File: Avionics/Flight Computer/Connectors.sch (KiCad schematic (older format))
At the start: 3 parts, among them J1 ERF8-040-05.0-S-DV-K, J2 ERF8-040-05.0-S-DV-K, J3 473460001

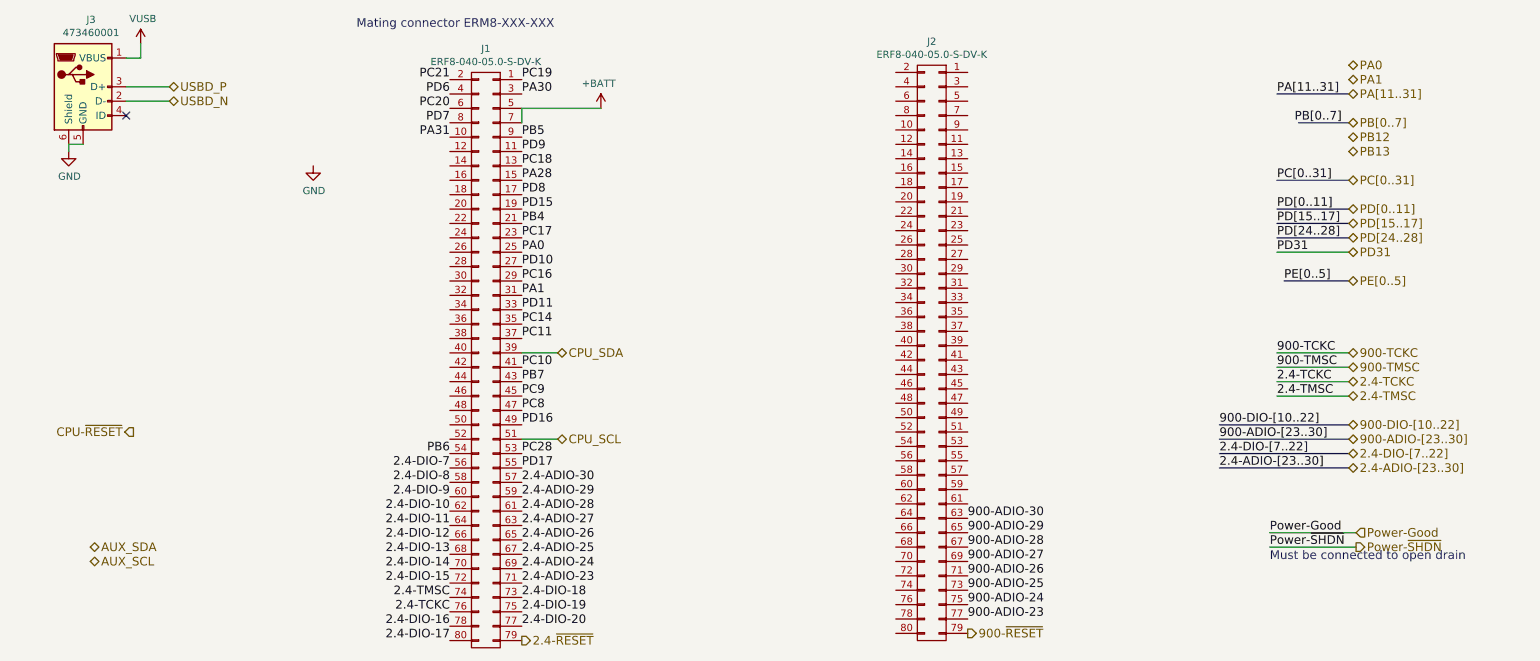
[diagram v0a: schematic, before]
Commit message: Additional routing
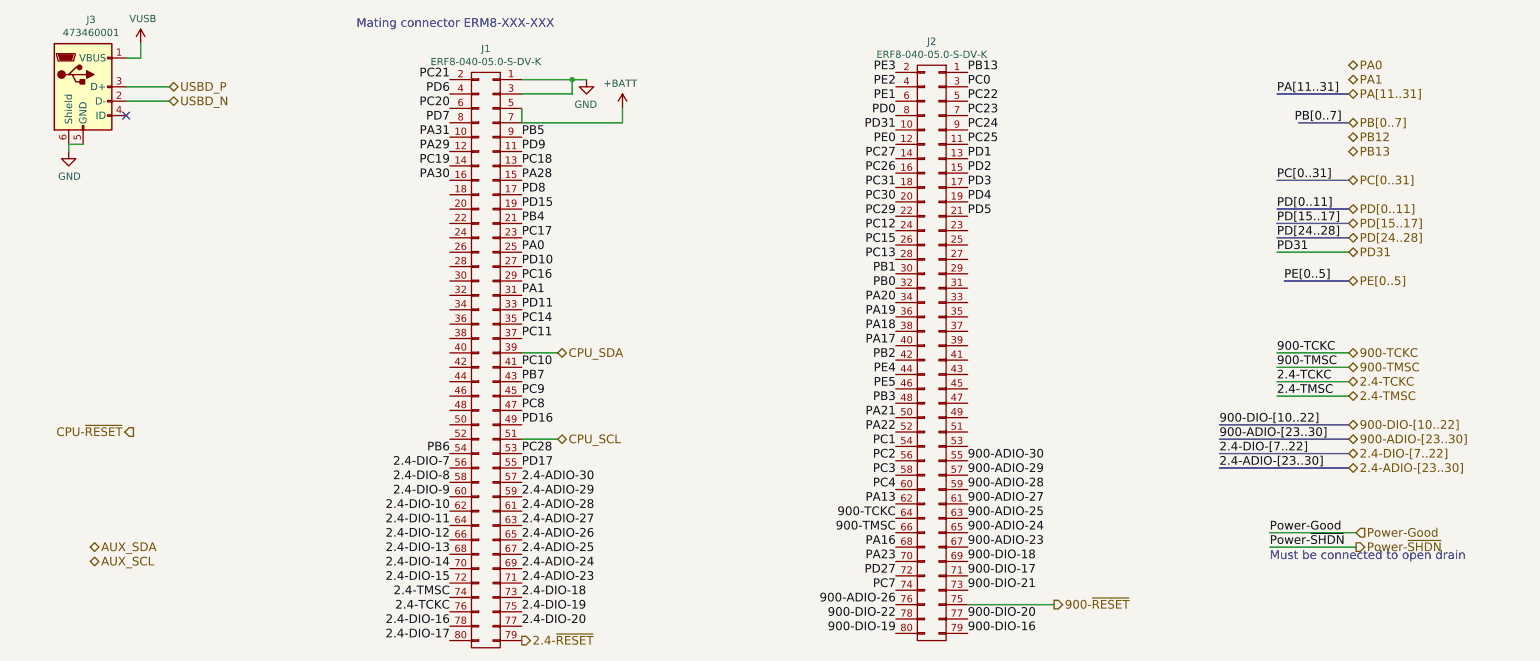
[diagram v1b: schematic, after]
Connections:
- net 900-ADIO-23: now also J2.67 (P67); no longer J2.77 (P77)
- net 900-ADIO-24: now also J2.65 (P65); no longer J2.75 (P75)
- net 900-ADIO-25: now also J2.63 (P63); no longer J2.73 (P73)
- net 900-ADIO-26: now also J2.76 (P76); no longer J2.71 (P71)
- net 900-ADIO-27: now also J2.61 (P61); no longer J2.69 (P69)
- net 900-ADIO-28: now also J2.59 (P59); no longer J2.67 (P67)
- net 900-ADIO-29: now also J2.57 (P57); no longer J2.65 (P65)
- net 900-ADIO-30: now also J2.55 (P55); no longer J2.63 (P63)
- net 900-TCKC: now also J2.64 (P64)
- net 900-TMSC: now also J2.66 (P66)
- net 900-~RESET: now also J2.75 (P75); no longer J2.79 (P79)
- net GND: now also J1.1 (P1), J1.3 (P3)
- net PA30: now also J1.16 (P16); no longer J1.3 (P3)
- net PB13: now also J2.1 (P1)
- net PC19: now also J1.14 (P14); no longer J1.1 (P1)
- net PD31: now also J2.10 (P10)
- net PC25: now reaches J2.11 (P11)
- net PE0: now reaches J2.12 (P12)
- net PD1: now reaches J2.13 (P13)
- net PC27: now reaches J2.14 (P14)
- net PD2: now reaches J2.15 (P15)
- net PC26: now reaches J2.16 (P16)
- net PD3: now reaches J2.17 (P17)
- net PC31: now reaches J2.18 (P18)
- net PD4: now reaches J2.19 (P19)
- net PE3: now reaches J2.2 (P2)
- net PC30: now reaches J2.20 (P20)
- net PD5: now reaches J2.21 (P21)
- net PC29: now reaches J2.22 (P22)
- net PC12: now reaches J2.24 (P24)
- net PC15: now reaches J2.26 (P26)
- net PC13: now reaches J2.28 (P28)
- net PC0: now reaches J2.3 (P3)
- net PB1: now reaches J2.30 (P30)
- net PB0: now reaches J2.32 (P32)
- net PA20: now reaches J2.34 (P34)
- net PA19: now reaches J2.36 (P36)
- net PA18: now reaches J2.38 (P38)
- net PE2: now reaches J2.4 (P4)
- net PA17: now reaches J2.40 (P40)
- net PB2: now reaches J2.42 (P42)
- net PE4: now reaches J2.44 (P44)
- net PE5: now reaches J2.46 (P46)
- net PB3: now reaches J2.48 (P48)
- net PC22: now reaches J2.5 (P5)
- net PA21: now reaches J2.50 (P50)
- net PA22: now reaches J2.52 (P52)
- net PC1: now reaches J2.54 (P54)
- net PC2: now reaches J2.56 (P56)
- net PC3: now reaches J2.58 (P58)
- net PE1: now reaches J2.6 (P6)
- net PC4: now reaches J2.60 (P60)
- net PA13: now reaches J2.62 (P62)
- net PA16: now reaches J2.68 (P68)
- net PC23: now reaches J2.7 (P7)
- net PA23: now reaches J2.70 (P70)
- net PD27: now reaches J2.72 (P72)
- net PC7: now reaches J2.74 (P74)
- net 900-DIO-22: now reaches J2.78 (P78)
- net PD0: now reaches J2.8 (P8)
- net 900-DIO-19: now reaches J2.80 (P80)
- net PC24: now reaches J2.9 (P9)
- net PA29: now reaches J1.12 (P12)
- new net 900-DIO-16: J2.79 (P79)
- new net 900-DIO-17: J2.71 (P71)
- new net 900-DIO-18: J2.69 (P69)
- new net 900-DIO-20: J2.77 (P77)
- new net 900-DIO-21: J2.73 (P73)
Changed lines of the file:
@@
 Text HLabel 1550 3850 0    60   Output ~ 0
 CPU-~RESET
-Text HLabel 7350 5250 2    60   Output ~ 0
+Text HLabel 7950 5050 2    60   Output ~ 0
 900-~RESET
 Text HLabel 4250 5300 2    60   Output ~ 0
@@
 Text Notes 9450 4750 0    60   ~ 0
 Must be connected to open drain\n
-Wire Wire Line
-	4800 1600 4250 1600
 $Comp
 L +BATT #PWR0118
 U 1 1 58DB91A4
-P 4800 1600
-F 0 "#PWR0118" H 3750 -1300 50  0001 C CNN
-F 1 "+BATT" H 4815 1773 50  0000 C CNN
-F 2 "" H 3750 -1150 50  0001 C CNN
-F 3 "" H 3750 -1150 50  0001 C CNN
-	1    4800 1600
+P 4950 1600
+F 0 "#PWR0118" H 3900 -1300 50  0001 C CNN
+F 1 "+BATT" H 4965 1773 50  0000 C CNN
+F 2 "" H 3900 -1150 50  0001 C CNN
+F 3 "" H 3900 -1150 50  0001 C CNN
+	1    4950 1600
 	-1   0    0    -1
 $EndComp
@@
 L GND #PWR0119
 U 1 1 58DD26EA
-P 2800 2000
-F 0 "#PWR0119" H -1150 -1700 50  0001 C CNN
-F 1 "GND" H 2805 1827 50  0000 C CNN
-F 2 "" H -1150 -1450 50  0001 C CNN
-F 3 "" H -1150 -1450 50  0001 C CNN
-	1    2800 2000
-	1    0    0    -1
+P 4700 1400
+F 0 "#PWR0119" H 750 -2300 50  0001 C CNN
+F 1 "GND" H 4705 1227 50  0000 C CNN
+F 2 "" H 750 -2050 50  0001 C CNN
+F 3 "" H 750 -2050 50  0001 C CNN
+	1    4700 1400
+	-1   0    0    -1
 $EndComp
+Text Label 7350 4150 0    60   ~ 0
+900-ADIO-29
+Text Label 7350 4050 0    60   ~ 0
+900-ADIO-30
+Text Label 7350 4250 0    60   ~ 0
+900-ADIO-28
+Text Label 6850 5050 2    60   ~ 0
+900-ADIO-26
 Text Label 7350 4550 0    60   ~ 0
-900-ADIO-29
+900-ADIO-24
+Text Label 7350 4650 0    60   ~ 0
+900-ADIO-23
+Text Label 7350 4350 0    60   ~ 0
+900-ADIO-27
 Text Label 7350 4450 0    60   ~ 0
-900-ADIO-30
-Text Label 7350 4650 0    60   ~ 0
-900-ADIO-28
-Text Label 7350 4850 0    60   ~ 0
-900-ADIO-26
-Text Label 7350 5050 0    60   ~ 0
-900-ADIO-24
-Text Label 7350 5150 0    60   ~ 0
-900-ADIO-23
-Text Label 7350 4750 0    60   ~ 0
-900-ADIO-27
-Text Label 7350 4950 0    60   ~ 0
 900-ADIO-25
 Text Label 3750 4200 2    60   ~ 0
@@
 Text Label 4250 1800 0    60   ~ 0
 PB5
-Text Label 4250 1500 0    60   ~ 0
+Text Label 3750 2100 2    60   ~ 0
 PA30
-Text Label 4250 1400 0    60   ~ 0
+Text Label 3750 2000 2    60   ~ 0
 PC19
 Text Label 3750 1800 2    60   ~ 0
@@
 Text Label 3750 1400 2    60   ~ 0
 PC21
+Text Label 6850 1350 2    60   ~ 0
+PE3
+Text Label 6850 1450 2    60   ~ 0
+PE2
+Text Label 6850 1550 2    60   ~ 0
+PE1
+Text Label 6850 1650 2    60   ~ 0
+PD0
+Text Label 6850 1750 2    60   ~ 0
+PD31
+Text Label 6850 1850 2    60   ~ 0
+PE0
+Text Label 7350 1350 0    60   ~ 0
+PB13
+Text Label 7350 1450 0    60   ~ 0
+PC0
+Text Label 6850 1950 2    60   ~ 0
+PC27
+Text Label 6850 2050 2    60   ~ 0
+PC26
+Text Label 6850 2150 2    60   ~ 0
+PC31
+Text Label 6850 2250 2    60   ~ 0
+PC30
+Text Label 6850 2350 2    60   ~ 0
+PC29
+Text Label 6850 2450 2    60   ~ 0
+PC12
+Text Label 6850 2550 2    60   ~ 0
+PC15
+Text Label 6850 2650 2    60   ~ 0
+PC13
+Text Label 6850 2750 2    60   ~ 0
+PB1
+Text Label 6850 2850 2    60   ~ 0
+PB0
+Text Label 6850 2950 2    60   ~ 0
+PA20
+Text Label 6850 3050 2    60   ~ 0
+PA19
+Text Label 6850 3150 2    60   ~ 0
+PA18
+Text Label 6850 3250 2    60   ~ 0
+PA17
+Text Label 6850 3350 2    60   ~ 0
+PB2
+Text Label 6850 3450 2    60   ~ 0
+PE4
+Text Label 6850 3550 2    60   ~ 0
+PE5
+Text Label 6850 3650 2    60   ~ 0
+PB3
+Text Label 6850 3750 2    60   ~ 0
+PA21
+Text Label 7350 5250 0    60   ~ 0
+900-DIO-16
+Text Label 7350 5150 0    60   ~ 0
+900-DIO-20
+Wire Wire Line
+	7350 5050 7950 5050
+Text Label 7350 4950 0    60   ~ 0
+900-DIO-21
+Text Label 7350 4850 0    60   ~ 0
+900-DIO-17
+Text Label 7350 4750 0    60   ~ 0
+900-DIO-18
+Text Label 6850 5150 2    60   ~ 0
+900-DIO-22
+Text Label 6850 5250 2    60   ~ 0
+900-DIO-19
+Text Label 7350 1850 0    60   ~ 0
+PC25
+Text Label 7350 1950 0    60   ~ 0
+PD1
+Text Label 7350 2050 0    60   ~ 0
+PD2
+Text Label 7350 1750 0    60   ~ 0
+PC24
+Text Label 7350 2150 0    60   ~ 0
+PD3
+Text Label 7350 1650 0    60   ~ 0
+PC23
+Text Label 7350 2250 0    60   ~ 0
+PD4
+Text Label 7350 2350 0    60   ~ 0
+PD5
+Text Label 7350 1550 0    60   ~ 0
+PC22
+Text Label 3750 1900 2    60   ~ 0
+PA29
+Text Label 6850 3850 2    60   ~ 0
+PA22
+Text Label 6850 4350 2    60   ~ 0
+PA13
+Text Label 6850 3950 2    60   ~ 0
+PC1
+Text Label 6850 4050 2    60   ~ 0
+PC2
+Text Label 6850 4150 2    60   ~ 0
+PC3
+Text Label 6850 4250 2    60   ~ 0
+PC4
+Text Label 6850 4650 2    60   ~ 0
+PA16
+Text Label 6850 4450 2    60   ~ 0
+900-TCKC
+Text Label 6850 4550 2    60   ~ 0
+900-TMSC
+Text Label 6850 4750 2    60   ~ 0
+PA23
+Text Label 6850 4850 2    60   ~ 0
+PD27
+Text Label 6850 4950 2    60   ~ 0
+PC7
+Wire Wire Line
+	4600 1500 4250 1500
+Wire Wire Line
+	4250 1400 4700 1400
+Wire Wire Line
+	4600 1400 4600 1500
+Wire Wire Line
+	4250 1700 4950 1700
+Wire Wire Line
+	4950 1700 4950 1600
+Connection ~ 4600 1400
 $EndSCHEMATC

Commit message: Finished routing and DRC check.
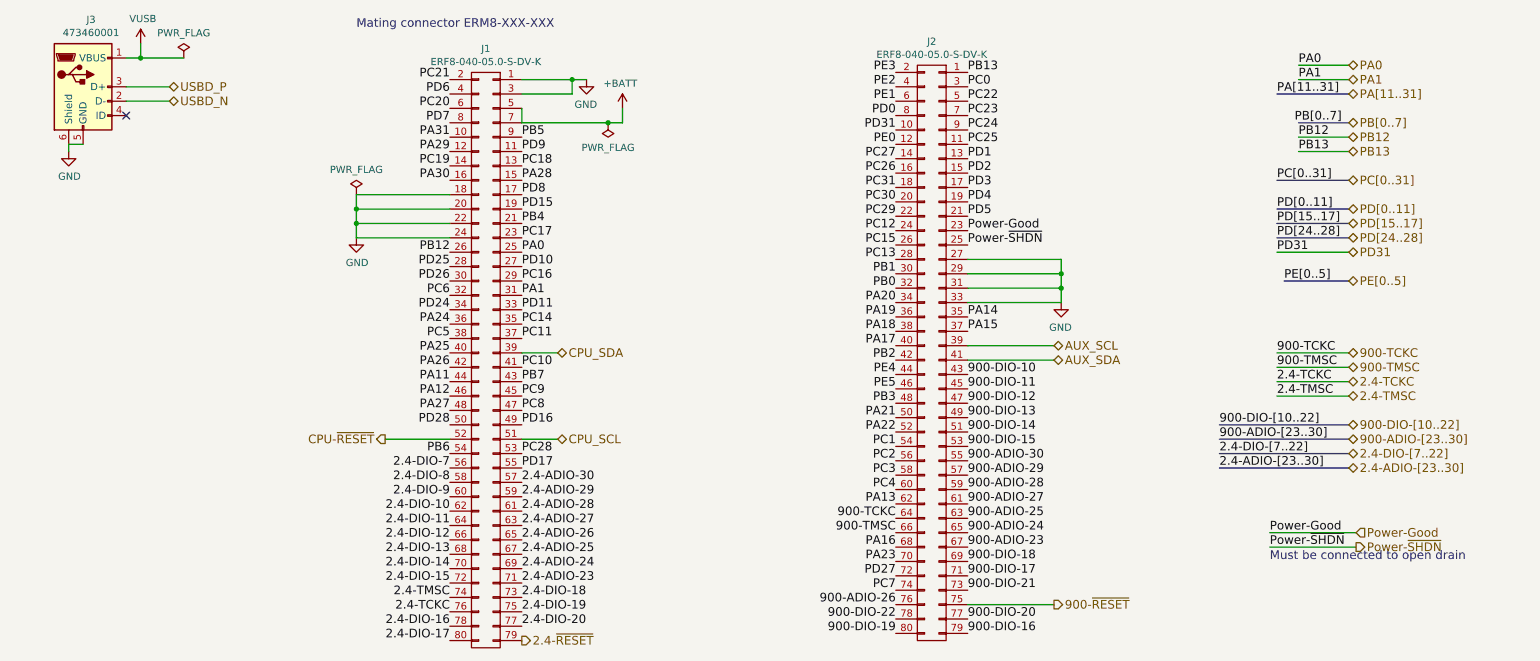
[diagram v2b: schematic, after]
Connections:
- net AUX_SCL: now also J2.39 (P39)
- net AUX_SDA: now also J2.41 (P41)
- net CPU-~RESET: now also J1.52 (P52)
- net GND: now also J1.18 (P18), J1.20 (P20), J1.22 (P22), J1.24 (P24), J2.27 (P27), J2.29 (P29), J2.31 (P31), J2.33 (P33)
- net PB12: now also J1.26 (P26)
- net Power-Good: now also J2.23 (P23)
- net Power-~SHDN: now also J2.25 (P25)
- net PA14: now reaches J2.35 (P35)
- net PA15: now reaches J2.37 (P37)
- net 900-DIO-10: now reaches J2.43 (P43)
- net 900-DIO-11: now reaches J2.45 (P45)
- net 900-DIO-12: now reaches J2.47 (P47)
- net 900-DIO-13: now reaches J2.49 (P49)
- net 900-DIO-14: now reaches J2.51 (P51)
- net 900-DIO-15: now reaches J2.53 (P53)
- net PD25: now reaches J1.28 (P28)
- net PD26: now reaches J1.30 (P30)
- net PC6: now reaches J1.32 (P32)
- net PD24: now reaches J1.34 (P34)
- net PA24: now reaches J1.36 (P36)
- net PC5: now reaches J1.38 (P38)
- net PA25: now reaches J1.40 (P40)
- net PA26: now reaches J1.42 (P42)
- net PA11: now reaches J1.44 (P44)
- net PA12: now reaches J1.46 (P46)
- net PA27: now reaches J1.48 (P48)
- net PD28: now reaches J1.50 (P50)
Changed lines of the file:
@@
 $EndComp
 $Comp
-L VUSB #PWR0116
+L VUSB #PWR0134
 U 1 1 58B8BBBA
 P 1600 1150
-F 0 "#PWR0116" H -400 -250 50  0001 C CNN
+F 0 "#PWR0134" H -400 -250 50  0001 C CNN
 F 1 "VUSB" H 1615 1323 50  0000 C CNN
 F 2 "" H -400 -100 50  0001 C CNN
@@
 $EndComp
 Wire Wire Line
-	1500 1250 1600 1250
+	1500 1250 1900 1250
 Wire Wire Line
 	1600 1250 1600 1150
 $Comp
-L GND #PWR0117
+L GND #PWR0135
 U 1 1 58B8BD69
 P 1100 1900
-F 0 "#PWR0117" H -800 50  50  0001 C CNN
+F 0 "#PWR0135" H -800 50  50  0001 C CNN
 F 1 "GND" H 1105 1727 50  0000 C CNN
 F 2 "" H -800 300 50  0001 C CNN
@@
 Text HLabel 1800 1550 2    60   BiDi ~ 0
 USBD_N
-Text HLabel 1550 3850 0    60   Output ~ 0
+Text HLabel 3300 3900 0    60   Output ~ 0
 CPU-~RESET
 Text HLabel 7950 5050 2    60   Output ~ 0
@@
 Text HLabel 10000 2600 2    60   BiDi ~ 0
 PD31
-Text HLabel 1250 4650 2    60   BiDi ~ 0
+Text HLabel 7950 3350 2    60   BiDi ~ 0
 AUX_SDA
-Text HLabel 1250 4750 2    60   BiDi ~ 0
+Text HLabel 7950 3250 2    60   BiDi ~ 0
 AUX_SCL
 Text HLabel 4500 3300 2    60   BiDi ~ 0
@@
 Must be connected to open drain\n
 $Comp
-L +BATT #PWR0118
+L +BATT #PWR0136
 U 1 1 58DB91A4
 P 4950 1600
-F 0 "#PWR0118" H 3900 -1300 50  0001 C CNN
+F 0 "#PWR0136" H 3900 -1300 50  0001 C CNN
 F 1 "+BATT" H 4965 1773 50  0000 C CNN
 F 2 "" H 3900 -1150 50  0001 C CNN
@@
 	9500 2600 10000 2600
 $Comp
-L GND #PWR0119
+L GND #PWR0137
 U 1 1 58DD26EA
 P 4700 1400
-F 0 "#PWR0119" H 750 -2300 50  0001 C CNN
+F 0 "#PWR0137" H 750 -2300 50  0001 C CNN
 F 1 "GND" H 4705 1227 50  0000 C CNN
 F 2 "" H 750 -2050 50  0001 C CNN
@@
 	4950 1700 4950 1600
 Connection ~ 4600 1400
+Text Label 7350 3450 0    60   ~ 0
+900-DIO-10
+Text Label 7350 3550 0    60   ~ 0
+900-DIO-11
+Text Label 7350 3650 0    60   ~ 0
+900-DIO-12
+Text Label 7350 3750 0    60   ~ 0
+900-DIO-13
+Text Label 7350 3850 0    60   ~ 0
+900-DIO-14
+Text Label 7350 3950 0    60   ~ 0
+900-DIO-15
+Wire Wire Line
+	7950 3250 7350 3250
+Wire Wire Line
+	7950 3350 7350 3350
+Wire Wire Line
+	3750 3900 3300 3900
+Text Label 3750 3800 2    60   ~ 0
+PD28
+Text Label 3750 3700 2    60   ~ 0
+PA27
+Text Label 3750 3600 2    60   ~ 0
+PA12
+Text Label 3750 3500 2    60   ~ 0
+PA11
+Text Label 3750 3400 2    60   ~ 0
+PA26
+Text Label 3750 3300 2    60   ~ 0
+PA25
+Text Label 3750 3200 2    60   ~ 0
+PC5
+Text Label 3750 3100 2    60   ~ 0
+PA24
+Text Label 3750 3000 2    60   ~ 0
+PD24
+Text Label 3750 2900 2    60   ~ 0
+PC6
+Text Label 3750 2800 2    60   ~ 0
+PD26
+Text Label 3750 2700 2    60   ~ 0
+PD25
+Text Label 7350 3050 0    60   ~ 0
+PA14
+Text Label 7350 3150 0    60   ~ 0
+PA15
+Wire Wire Line
+	9650 1800 10000 1800
+Wire Wire Line
+	10000 1900 9650 1900
+Wire Wire Line
+	10000 1400 9650 1400
+Wire Wire Line
+	10000 1300 9650 1300
+Text Label 9650 1300 0    60   ~ 0
+PA0
+Text Label 9650 1400 0    60   ~ 0
+PA1
+Text Label 9650 1800 0    60   ~ 0
+PB12
+Text Label 9650 1900 0    60   ~ 0
+PB13
+Text Label 3750 2600 2    60   ~ 0
+PB12
+Text Label 7350 2450 0    60   ~ 0
+Power-Good
+Text Label 7350 2550 0    60   ~ 0
+Power-~SHDN
+Wire Wire Line
+	7350 2650 8000 2650
+Wire Wire Line
+	8000 2650 8000 2950
+Wire Wire Line
+	8000 2950 7350 2950
+Wire Wire Line
+	8000 2850 7350 2850
+Connection ~ 8000 2850
+Wire Wire Line
+	7350 2750 8000 2750
+Connection ~ 8000 2750
+$Comp
+L GND #PWR0138
+U 1 1 58BDD19A
+P 8000 2950
+F 0 "#PWR0138" H 4050 -750 50  0001 C CNN
+F 1 "GND" H 8005 2777 50  0000 C CNN
+F 2 "" H 4050 -500 50  0001 C CNN
+F 3 "" H 4050 -500 50  0001 C CNN
+	1    8000 2950
+	-1   0    0    -1
+$EndComp
+Wire Wire Line
+	3750 2200 3100 2200
+Wire Wire Line
+	3100 2200 3100 2500
+Wire Wire Line
+	3100 2500 3750 2500
+Wire Wire Line
+	3100 2400 3750 2400
+Connection ~ 3100 2400
+Wire Wire Line
+	3750 2300 3100 2300
+Connection ~ 3100 2300
+$Comp
+L GND #PWR0139
+U 1 1 58BDD20C
+P 3100 2500
+F 0 "#PWR0139" H -850 -1200 50  0001 C CNN
+F 1 "GND" H 3105 2327 50  0000 C CNN
+F 2 "" H -850 -950 50  0001 C CNN
+F 3 "" H -850 -950 50  0001 C CNN
+	1    3100 2500
+	1    0    0    -1
+$EndComp
+$Comp
+L PWR_FLAG #FLG0140
+U 1 1 58BE5320
+P 4850 1700
+F 0 "#FLG0140" H -800 275 50  0001 C CNN
+F 1 "PWR_FLAG" H 4850 1873 50  0000 C CNN
+F 2 "" H -800 200 50  0001 C CNN
+F 3 "" H -800 200 50  0001 C CNN
+	1    4850 1700
+	-1   0    0    1
+$EndComp
+Connection ~ 4850 1700
+$Comp
+L PWR_FLAG #FLG0141
+U 1 1 58BE5430
+P 1900 1250
+F 0 "#FLG0141" H -3750 -175 50  0001 C CNN
+F 1 "PWR_FLAG" H 1900 1424 50  0000 C CNN
+F 2 "" H -3750 -250 50  0001 C CNN
+F 3 "" H -3750 -250 50  0001 C CNN
+	1    1900 1250
+	1    0    0    -1
+$EndComp
+Connection ~ 1600 1250
+$Comp
+L PWR_FLAG #FLG0142
+U 1 1 58BEF4A7
+P 3100 2200
+F 0 "#FLG0142" H -2550 775 50  0001 C CNN
+F 1 "PWR_FLAG" H 3100 2374 50  0000 C CNN
+F 2 "" H -2550 700 50  0001 C CNN
+F 3 "" H -2550 700 50  0001 C CNN
+	1    3100 2200
+	1    0    0    -1
+$EndComp
 $EndSCHEMATC

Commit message: Fixed some grounding and routing. Moved USB input diode to top side to make reduced BOM easier.
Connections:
- net GND: no longer J1.18 (P18), J1.20 (P20), J2.27 (P27), J2.29 (P29)
- new net +3V3: J1.18 (P18), J1.20 (P20), J2.27 (P27), J2.29 (P29)
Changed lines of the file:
@@
 Power-~SHDN
 Wire Wire Line
-	7350 2650 8000 2650
+	7350 2650 8150 2650
 Wire Wire Line
-	8000 2650 8000 2950
+	8150 2850 8150 2950
 Wire Wire Line
-	8000 2950 7350 2950
+	8150 2950 7350 2950
 Wire Wire Line
-	8000 2850 7350 2850
-Connection ~ 8000 2850
+	8150 2850 7350 2850
 Wire Wire Line
-	7350 2750 8000 2750
-Connection ~ 8000 2750
+	7350 2750 8150 2750
 $Comp
 L GND #PWR0138
 U 1 1 58BDD19A
-P 8000 2950
-F 0 "#PWR0138" H 4050 -750 50  0001 C CNN
-F 1 "GND" H 8005 2777 50  0000 C CNN
-F 2 "" H 4050 -500 50  0001 C CNN
-F 3 "" H 4050 -500 50  0001 C CNN
-	1    8000 2950
+P 8150 2950
+F 0 "#PWR0138" H 4200 -750 50  0001 C CNN
+F 1 "GND" H 8155 2777 50  0000 C CNN
+F 2 "" H 4200 -500 50  0001 C CNN
+F 3 "" H 4200 -500 50  0001 C CNN
+	1    8150 2950
 	-1   0    0    -1
 $EndComp
 Wire Wire Line
 	3750 2200 3100 2200
-Wire Wire Line
-	3100 2200 3100 2500
 Wire Wire Line
 	3100 2500 3750 2500
@@
 L PWR_FLAG #FLG0142
 U 1 1 58BEF4A7
+P 3100 2400
+F 0 "#FLG0142" H -2550 975 50  0001 C CNN
+F 1 "PWR_FLAG" V 3100 2528 50  0000 L CNN
+F 2 "" H -2550 900 50  0001 C CNN
+F 3 "" H -2550 900 50  0001 C CNN
+	1    3100 2400
+	0    -1   -1   0
+$EndComp
+Wire Wire Line
+	3100 2500 3100 2400
+Wire Wire Line
+	3100 2300 3100 2200
+$Comp
+L +3.3V #PWR?
+U 1 1 58BFD0A3
 P 3100 2200
-F 0 "#FLG0142" H -2550 775 50  0001 C CNN
-F 1 "PWR_FLAG" H 3100 2374 50  0000 C CNN
-F 2 "" H -2550 700 50  0001 C CNN
-F 3 "" H -2550 700 50  0001 C CNN
+F 0 "#PWR?" H 100 100 50  0001 C CNN
+F 1 "+3.3V" H 3115 2373 50  0000 C CNN
+F 2 "" H 100 250 50  0001 C CNN
+F 3 "" H 100 250 50  0001 C CNN
 	1    3100 2200
 	1    0    0    -1
 $EndComp
+$Comp
+L +3.3V #PWR?
+U 1 1 58BFD1FD
+P 8150 2650
+F 0 "#PWR?" H 5150 550 50  0001 C CNN
+F 1 "+3.3V" H 8165 2823 50  0000 C CNN
+F 2 "" H 5150 700 50  0001 C CNN
+F 3 "" H 5150 700 50  0001 C CNN
+	1    8150 2650
+	1    0    0    -1
+$EndComp
+Wire Wire Line
+	8150 2750 8150 2650
 $EndSCHEMATC
